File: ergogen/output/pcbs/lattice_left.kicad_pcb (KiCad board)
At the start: 2 copper layers, 114.3 x 85.7 mm, 48 parts

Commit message: matrix finished
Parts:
- added J1: , USB_C_Receptacle, B.Cu at (95.2, 40.3)
- added J2: , USB_C_Receptacle, B.Cu at (190.5, 40.3)
- added U1: , RP2040, B.Cu at (152.4, 47.6)
- moved D1 4.76 mm to (87.6, 114.3)
- moved D10 4.76 mm to (125.7, 95.2)
- moved D11 4.76 mm to (125.7, 76.2)
- moved D12 4.76 mm to (125.7, 57.2)
- moved D13 4.76 mm to (144.8, 114.3)
- moved D14 4.76 mm to (144.8, 95.2)
- moved D15 4.76 mm to (144.8, 76.2)
- moved D16 4.76 mm to (144.8, 57.2)
- moved D17 4.76 mm to (163.8, 114.3)
- moved D18 4.76 mm to (163.8, 95.2)
- moved D19 4.76 mm to (163.8, 76.2)
- moved D2 4.76 mm to (87.6, 95.2)
- moved D20 4.76 mm to (163.8, 57.2)
- moved D21 4.76 mm to (182.9, 114.3)
- moved D22 4.76 mm to (182.9, 95.2)
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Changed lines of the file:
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@@
         )
         (module 1N4148W (layer B.Cu)
-            (at 87.63 109.5375 270)
+            (at 87.63 114.3 270)
             (fp_text reference "D1" (at 0 0 0) (layer "B.Fab")
               (effects (font (size 1 1) (thickness 0.15)))
@@
         )
         (module 1N4148W (layer B.Cu)
-            (at 87.63 90.4875 270)
+            (at 87.63 95.25 270)
             (fp_text reference "D2" (at 0 0 0) (layer "B.Fab")
               (effects (font (size 1 1) (thickness 0.15)))
@@
         )
         (module 1N4148W (layer B.Cu)
-            (at 87.63 71.4375 270)
+            (at 87.63 76.2 270)
             (fp_text reference "D3" (at 0 0 0) (layer "B.Fab")
               (effects (font (size 1 1) (thickness 0.15)))
@@
         )
         (module 1N4148W (layer B.Cu)
-            (at 87.63 52.3875 270)
+            (at 87.63 57.150000000000006 270)
             (fp_text reference "D4" (at 0 0 0) (layer "B.Fab")
               (effects (font (size 1 1) (thickness 0.15)))
@@
         )
         (module 1N4148W (layer B.Cu)
-            (at 106.67999999999999 109.5375 270)
+            (at 106.67999999999999 114.3 270)
             (fp_text reference "D5" (at 0 0 0) (layer "B.Fab")
               (effects (font (size 1 1) (thickness 0.15)))
@@
         )
         (module 1N4148W (layer B.Cu)
-            (at 106.67999999999999 90.4875 270)
+            (at 106.67999999999999 95.25 270)
             (fp_text reference "D6" (at 0 0 0) (layer "B.Fab")
               (effects (font (size 1 1) (thickness 0.15)))
@@
         )
         (module 1N4148W (layer B.Cu)
-            (at 106.67999999999999 71.4375 270)
+            (at 106.67999999999999 76.2 270)
             (fp_text reference "D7" (at 0 0 0) (layer "B.Fab")
               (effects (font (size 1 1) (thickness 0.15)))
@@
         )
         (module 1N4148W (layer B.Cu)
-            (at 106.67999999999999 52.3875 270)
+            (at 106.67999999999999 57.150000000000006 270)
             (fp_text reference "D8" (at 0 0 0) (layer "B.Fab")
               (effects (font (size 1 1) (thickness 0.15)))
@@
         )
         (module 1N4148W (layer B.Cu)
-            (at 125.72999999999999 109.5375 270)
+            (at 125.72999999999999 114.3 270)
             (fp_text reference "D9" (at 0 0 0) (layer "B.Fab")
               (effects (font (size 1 1) (thickness 0.15)))
@@
         )
         (module 1N4148W (layer B.Cu)
-            (at 125.72999999999999 90.4875 270)
+            (at 125.72999999999999 95.25 270)
             (fp_text reference "D10" (at 0 0 0) (layer "B.Fab")
               (effects (font (size 1 1) (thickness 0.15)))
@@
         )
         (module 1N4148W (layer B.Cu)
-            (at 125.72999999999999 71.4375 270)
+            (at 125.72999999999999 76.2 270)
             (fp_text reference "D11" (at 0 0 0) (layer "B.Fab")
               (effects (font (size 1 1) (thickness 0.15)))
@@
         )
         (module 1N4148W (layer B.Cu)
-            (at 125.72999999999999 52.3875 270)
+            (at 125.72999999999999 57.150000000000006 270)
             (fp_text reference "D12" (at 0 0 0) (layer "B.Fab")
               (effects (font (size 1 1) (thickness 0.15)))
@@
         )
         (module 1N4148W (layer B.Cu)
-            (at 144.78 109.5375 270)
+            (at 144.78 114.3 270)
             (fp_text reference "D13" (at 0 0 0) (layer "B.Fab")
               (effects (font (size 1 1) (thickness 0.15)))
@@
         )
         (module 1N4148W (layer B.Cu)
-            (at 144.78 90.4875 270)
+            (at 144.78 95.25 270)
             (fp_text reference "D14" (at 0 0 0) (layer "B.Fab")
               (effects (font (size 1 1) (thickness 0.15)))
@@
         )
         (module 1N4148W (layer B.Cu)
-            (at 144.78 71.4375 270)
+            (at 144.78 76.2 270)
             (fp_text reference "D15" (at 0 0 0) (layer "B.Fab")
               (effects (font (size 1 1) (thickness 0.15)))
@@
         )
         (module 1N4148W (layer B.Cu)
-            (at 144.78 52.3875 270)
+            (at 144.78 57.150000000000006 270)
             (fp_text reference "D16" (at 0 0 0) (layer "B.Fab")
               (effects (font (size 1 1) (thickness 0.15)))
@@
         )
         (module 1N4148W (layer B.Cu)
-            (at 163.82999999999998 109.5375 270)
+            (at 163.82999999999998 114.3 270)
             (fp_text reference "D17" (at 0 0 0) (layer "B.Fab")
               (effects (font (size 1 1) (thickness 0.15)))
@@
         )
         (module 1N4148W (layer B.Cu)
-            (at 163.82999999999998 90.4875 270)
+            (at 163.82999999999998 95.25 270)
             (fp_text reference "D18" (at 0 0 0) (layer "B.Fab")
               (effects (font (size 1 1) (thickness 0.15)))
@@
         )
         (module 1N4148W (layer B.Cu)
-            (at 163.82999999999998 71.4375 270)
+            (at 163.82999999999998 76.2 270)
             (fp_text reference "D19" (at 0 0 0) (layer "B.Fab")
               (effects (font (size 1 1) (thickness 0.15)))
@@
         )
         (module 1N4148W (layer B.Cu)
-            (at 163.82999999999998 52.3875 270)
+            (at 163.82999999999998 57.150000000000006 270)
             (fp_text reference "D20" (at 0 0 0) (layer "B.Fab")
               (effects (font (size 1 1) (thickness 0.15)))
@@
         )
         (module 1N4148W (layer B.Cu)
-            (at 182.88 109.5375 270)
+            (at 182.88 114.3 270)
             (fp_text reference "D21" (at 0 0 0) (layer "B.Fab")
               (effects (font (size 1 1) (thickness 0.15)))
@@
         )
         (module 1N4148W (layer B.Cu)
-            (at 182.88 90.4875 270)
+            (at 182.88 95.25 270)
             (fp_text reference "D22" (at 0 0 0) (layer "B.Fab")
               (effects (font (size 1 1) (thickness 0.15)))
@@
         )
         (module 1N4148W (layer B.Cu)
-            (at 182.88 71.4375 270)
+            (at 182.88 76.2 270)
             (fp_text reference "D23" (at 0 0 0) (layer "B.Fab")
               (effects (font (size 1 1) (thickness 0.15)))
@@
         )
         (module 1N4148W (layer B.Cu)
-            (at 182.88 52.3875 270)
+            (at 182.88 57.150000000000006 270)
             (fp_text reference "D24" (at 0 0 0) (layer "B.Fab")
               (effects (font (size 1 1) (thickness 0.15)))
             )
+        )
+        (module USB_C_Receptacle (layer B.Cu)
+            (at 95.25 40.300000000000004 0)
+            (fp_text reference "J1" (at 0 0 0) (layer "B.Fab")
+              (effects (font (size 1 1) (thickness 0.15)))
+            )
+        )
+        (module USB_C_Receptacle (layer B.Cu)
+            (at 190.5 40.300000000000004 0)
+            (fp_text reference "J2" (at 0 0 0) (layer "B.Fab")
+              (effects (font (size 1 1) (thickness 0.15)))
+            )
+        )
+        (module RP2040 (layer B.Cu)
+            (at 152.4 47.62500000000001 45)
+            (fp_text reference "U1" (at 0 0 0) (layer "B.Fab")
+              (effects (font (size 1 1) (thickness 0.15)))
+            )

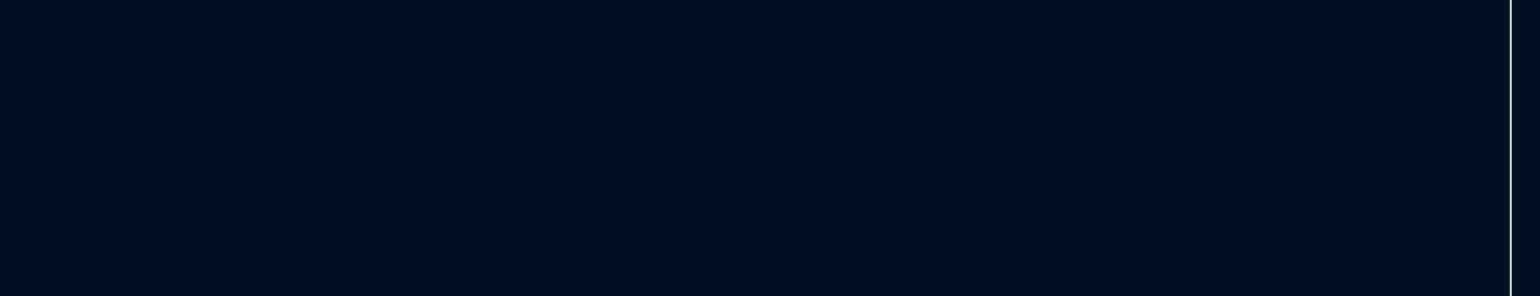
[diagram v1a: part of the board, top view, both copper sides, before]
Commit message: silkscreen text
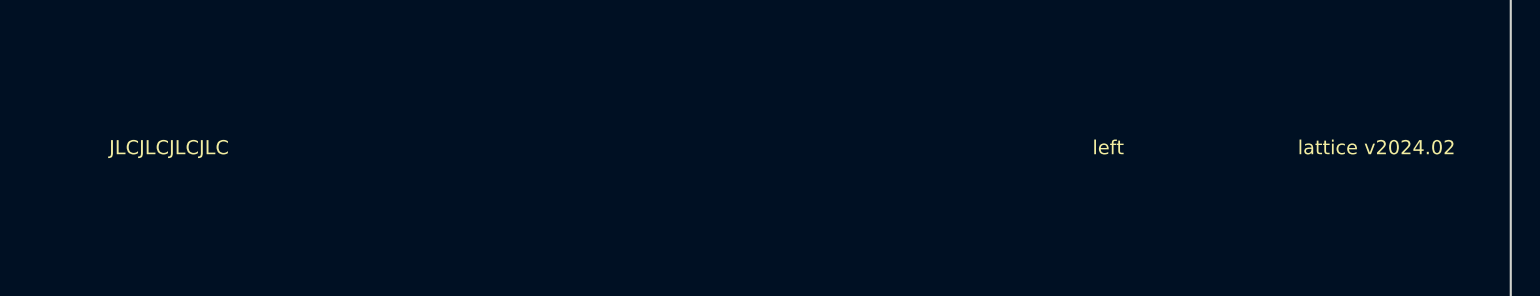
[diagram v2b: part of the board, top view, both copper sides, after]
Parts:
- moved U1 2.38 mm to (152.4, 45.2)
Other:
- board text added: "JLCJLCJLCJLC"
- board text added: "lattice v2024.02"
- board text added: "left"
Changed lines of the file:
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@@
         )
         (module RP2040 (layer B.Cu)
-            (at 152.4 47.62500000000001 45)
+            (at 152.4 45.243750000000006 45)
             (fp_text reference "U1" (at 0 0 0) (layer "B.Fab")
               (effects (font (size 1 1) (thickness 0.15)))
             )
         )
+            (gr_text "JLCJLCJLCJLC" (at 104.775 104.77499999999999 0) (layer F.SilkS)
+                (effects (font (size 1 1) (thickness 0.15)) )
+            )
+            (gr_text "left" (at 171.45 104.77499999999999 0) (layer F.SilkS)
+                (effects (font (size 1 1) (thickness 0.15)) )
+            )
+            (gr_text "lattice v2024.02" (at 190.5 104.77499999999999 0) (layer F.SilkS)
+                (effects (font (size 1 1) (thickness 0.15)) )
+            )
   (gr_line (start 85.725 120.825) (end 85.725 41.10000000000001) (angle 90) (layer Edge.Cuts) (width 0.15))
 (gr_line (start 88.725 38.10000000000001) (end 197.025 38.10000000000001) (angle 90) (layer Edge.Cuts) (width 0.15))

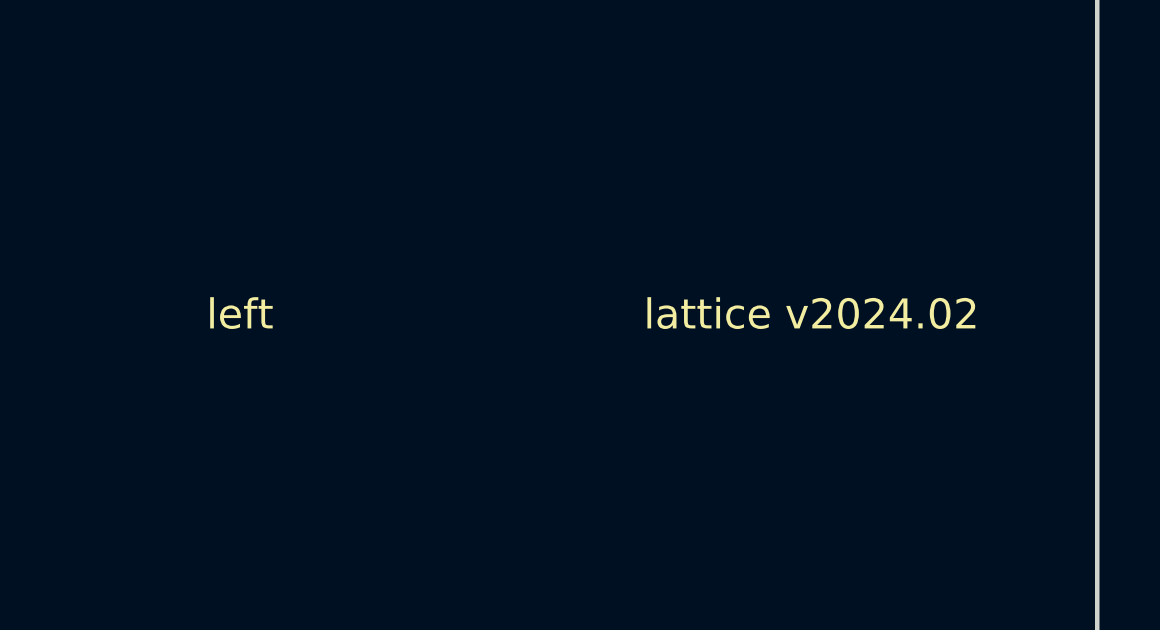
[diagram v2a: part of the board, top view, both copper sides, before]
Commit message: placing major rp2040 components
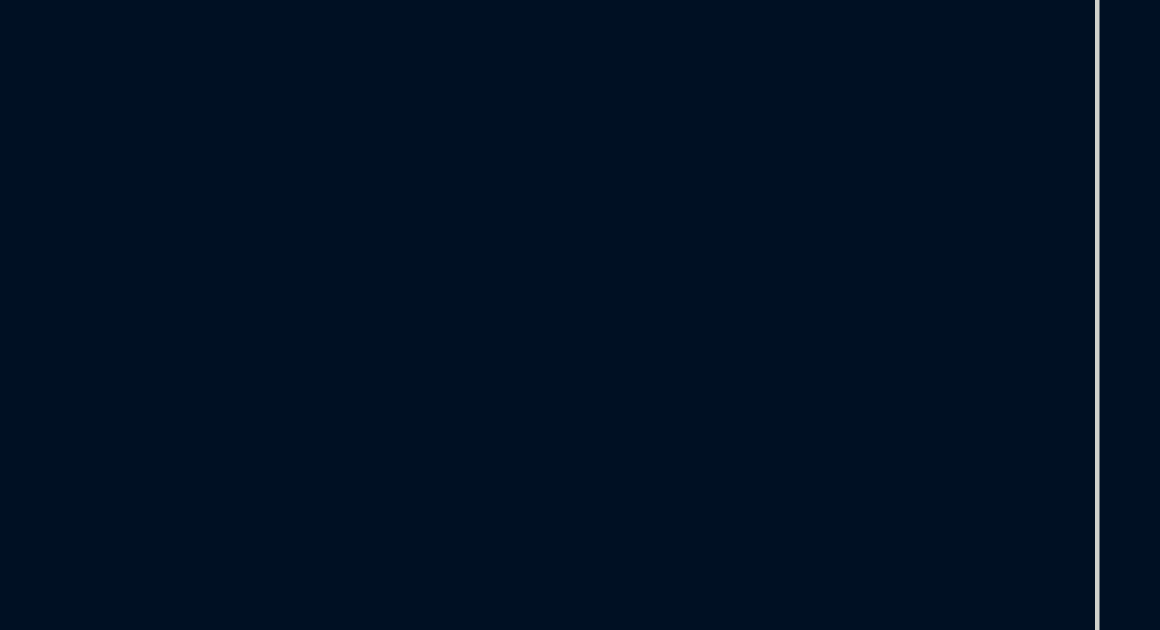
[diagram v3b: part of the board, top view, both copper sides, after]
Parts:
- added F1: , Polyfuse_Small, B.Cu at (104.8, 45.2)
- added SYM1: , Logo_Open_Hardware_Small, B.Cu at (142.9, 104.8)
- added U2: , W25Q128JVS, B.Cu at (114.3, 45.2)
- added U3: , USBLC6-2SC6, B.Cu at (133.3, 45.2)
- added U4: , XC6206PxxxMR, B.Cu at (166.7, 45.2)
- added Y1: , Crystal_GND24_Small, B.Cu at (176.2, 45.2)
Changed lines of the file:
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@@
+            )
+        )
+        (module W25Q128JVS (layer B.Cu)
+            (at 114.3 45.243750000000006 0)
+            (fp_text reference "U2" (at 0 0 0) (layer "B.Fab")
+              (effects (font (size 1 1) (thickness 0.15)))
+            )
+        )
+        (module USBLC6-2SC6 (layer B.Cu)
+            (at 133.35 45.243750000000006 0)
+            (fp_text reference "U3" (at 0 0 0) (layer "B.Fab")
+              (effects (font (size 1 1) (thickness 0.15)))
+            )
+        )
+        (module XC6206PxxxMR (layer B.Cu)
+            (at 166.6875 45.243750000000006 0)
+            (fp_text reference "U4" (at 0 0 0) (layer "B.Fab")
+              (effects (font (size 1 1) (thickness 0.15)))
+            )
+        )
+        (module Crystal_GND24_Small (layer B.Cu)
+            (at 176.21249999999998 45.243750000000006 0)
+            (fp_text reference "Y1" (at 0 0 0) (layer "B.Fab")
+              (effects (font (size 1 1) (thickness 0.15)))
+            )
+        )
+        (module Polyfuse_Small (layer B.Cu)
+            (at 104.775 45.243750000000006 90)
+            (fp_text reference "F1" (at 0 0 0) (layer "B.Fab")
+              (effects (font (size 1 1) (thickness 0.15)))
+            )
+        )
+        (module Logo_Open_Hardware_Small (layer B.Cu)
+            (at 142.875 104.77499999999999 180)
+            (fp_text reference "SYM1" (at 0 0 0) (layer "B.Fab")
+              (effects (font (size 1 1) (thickness 0.15)))
             )
         )
@@
                 (effects (font (size 1 1) (thickness 0.15)) )
             )
-            (gr_text "left" (at 171.45 104.77499999999999 0) (layer F.SilkS)
-                (effects (font (size 1 1) (thickness 0.15)) )
+            (gr_text "left" (at 104.775 104.77499999999999 0) (layer B.SilkS knockout)
+                (effects (font  (face "JetBrainsMono NF") (size 1 1) (thickness 0.15)) (justify mirror))
             )
-            (gr_text "lattice v2024.02" (at 190.5 104.77499999999999 0) (layer F.SilkS)
-                (effects (font (size 1 1) (thickness 0.15)) )
+            (gr_text "lattice v2024.02" (at 180.975 104.77499999999999 0) (layer B.SilkS knockout)
+                (effects (font  (face "JetBrainsMono NF") (size 1 1) (thickness 0.15)) (justify mirror))
             )
   (gr_line (start 85.725 120.825) (end 85.725 41.10000000000001) (angle 90) (layer Edge.Cuts) (width 0.15))

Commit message: more work on schematic
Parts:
- added R1: , 5k1, B.Cu at (88.2, 46.6)
- added R2: , 5k1, B.Cu at (88.2, 48.6)
- F1: footprint Polyfuse_Small -> 500mA
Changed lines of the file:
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@@
             )
         )
-        (module Polyfuse_Small (layer B.Cu)
+        (module 500mA (layer B.Cu)
             (at 104.775 45.243750000000006 90)
             (fp_text reference "F1" (at 0 0 0) (layer "B.Fab")
               (effects (font (size 1 1) (thickness 0.15)))
             )
+        )
+        (module 5k1 (layer B.Cu)
+            (at 88.25 46.62500000000001 180)
+            (fp_text reference "R1" (at 0 0 0) (layer "B.Fab")
+              (effects (font (size 1 1) (thickness 0.15)))
+            )
+        )
+        (module 5k1 (layer B.Cu)
+            (at 88.25 48.62500000000001 180)
+            (fp_text reference "R2" (at 0 0 0) (layer "B.Fab")
+              (effects (font (size 1 1) (thickness 0.15)))
+            )

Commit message: schematic done, most components placed
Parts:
- added C1: , 1uF, B.Cu at (116.5, 42.9)
- added C2: , 1uF, B.Cu at (118.5, 42.9)
- added C3: , 100nF, B.Cu at (161.9, 48.8)
- added C4: , 22pF, B.Cu at (180.0, 42.9)
- added C5: , 22pF, B.Cu at (182.0, 42.9)
- added R3: , 1k, B.Cu at (166.7, 47.6)
- added R4: , 1k, B.Cu at (176.2, 47.6)
- added SW1: , SW_Push, B.Cu at (128.6, 47.6)
- added SW2: , SW_Push, B.Cu at (138.1, 47.6)
- Y1: footprint Crystal_GND24_Small -> 12MHz
- moved U3 24.0 mm to (109.5, 47.9), turned to 90 degrees
- moved U2 5.32 mm to (109.5, 42.9), turned to 90 degrees
- moved F1 3.47 mm to (102.2, 42.9)
- moved U4 2.38 mm to (166.7, 42.9)
- moved Y1 2.38 mm to (176.2, 42.9)
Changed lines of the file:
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@@
+            )
+        )
+        (module 500mA (layer B.Cu)
+            (at 102.25 42.862500000000004 90)
+            (fp_text reference "F1" (at 0 0 0) (layer "B.Fab")
+              (effects (font (size 1 1) (thickness 0.15)))
+            )
+        )
+        (module 5k1 (layer B.Cu)
+            (at 88.25 46.62500000000001 180)
+            (fp_text reference "R1" (at 0 0 0) (layer "B.Fab")
+              (effects (font (size 1 1) (thickness 0.15)))
+            )
+        )
+        (module 5k1 (layer B.Cu)
+            (at 88.25 48.62500000000001 180)
+            (fp_text reference "R2" (at 0 0 0) (layer "B.Fab")
+              (effects (font (size 1 1) (thickness 0.15)))
             )
         )
@@
         )
         (module W25Q128JVS (layer B.Cu)
-            (at 114.3 45.243750000000006 0)
+            (at 109.5375 42.862500000000004 90)
             (fp_text reference "U2" (at 0 0 0) (layer "B.Fab")
               (effects (font (size 1 1) (thickness 0.15)))
             )
         )
+        (module 1uF (layer B.Cu)
+            (at 116.475 42.862500000000004 90)
+            (fp_text reference "C1" (at 0 0 0) (layer "B.Fab")
+              (effects (font (size 1 1) (thickness 0.15)))
+            )
+        )
+        (module 1uF (layer B.Cu)
+            (at 118.475 42.862500000000004 90)
+            (fp_text reference "C2" (at 0 0 0) (layer "B.Fab")
+              (effects (font (size 1 1) (thickness 0.15)))
+            )
+        )
         (module USBLC6-2SC6 (layer B.Cu)
-            (at 133.35 45.243750000000006 0)
+            (at 109.5375 47.862500000000004 90)
             (fp_text reference "U3" (at 0 0 0) (layer "B.Fab")
               (effects (font (size 1 1) (thickness 0.15)))
@@
         )
         (module XC6206PxxxMR (layer B.Cu)
-            (at 166.6875 45.243750000000006 0)
+            (at 166.6875 42.862500000000004 0)
             (fp_text reference "U4" (at 0 0 0) (layer "B.Fab")
               (effects (font (size 1 1) (thickness 0.15)))
             )
         )
-        (module Crystal_GND24_Small (layer B.Cu)
-            (at 176.21249999999998 45.243750000000006 0)
+        (module 100nF (layer B.Cu)
+            (at 161.925 48.815625000000004 90)
+            (fp_text reference "C3" (at 0 0 0) (layer "B.Fab")
+              (effects (font (size 1 1) (thickness 0.15)))
+            )
+        )
+        (module 1k (layer B.Cu)
+            (at 166.6875 47.62500000000001 0)
+            (fp_text reference "R3" (at 0 0 0) (layer "B.Fab")
+              (effects (font (size 1 1) (thickness 0.15)))
+            )
+        )
+        (module 12MHz (layer B.Cu)
+            (at 176.21249999999998 42.862500000000004 0)
             (fp_text reference "Y1" (at 0 0 0) (layer "B.Fab")
               (effects (font (size 1 1) (thickness 0.15)))
             )
         )
-        (module 500mA (layer B.Cu)
-            (at 104.775 45.243750000000006 90)
-            (fp_text reference "F1" (at 0 0 0) (layer "B.Fab")
+        (module 22pF (layer B.Cu)
+            (at 179.975 42.862500000000004 90)
+            (fp_text reference "C4" (at 0 0 0) (layer "B.Fab")
               (effects (font (size 1 1) (thickness 0.15)))
             )
         )
-        (module 5k1 (layer B.Cu)
-            (at 88.25 46.62500000000001 180)
-            (fp_text reference "R1" (at 0 0 0) (layer "B.Fab")
+        (module 22pF (layer B.Cu)
+            (at 181.975 42.862500000000004 90)
+            (fp_text reference "C5" (at 0 0 0) (layer "B.Fab")
               (effects (font (size 1 1) (thickness 0.15)))
             )
         )
-        (module 5k1 (layer B.Cu)
-            (at 88.25 48.62500000000001 180)
-            (fp_text reference "R2" (at 0 0 0) (layer "B.Fab")
+        (module 1k (layer B.Cu)
+            (at 176.21249999999998 47.62500000000001 0)
+            (fp_text reference "R4" (at 0 0 0) (layer "B.Fab")
               (effects (font (size 1 1) (thickness 0.15)))
             )
+        )
+        (module SW_Push (layer B.Cu)
+            (at 128.5875 47.62500000000001 90)
+            (fp_text reference "SW1" (at 0 0 0) (layer "B.Fab")
+              (effects (font (size 1 1) (thickness 0.15)))
+            )
+        )
+        (module SW_Push (layer B.Cu)
+            (at 138.11249999999998 47.62500000000001 90)
+            (fp_text reference "SW2" (at 0 0 0) (layer "B.Fab")
+              (effects (font (size 1 1) (thickness 0.15)))
+            )
